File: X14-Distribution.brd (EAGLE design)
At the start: 152.4 x 76.2 mm, 57 parts, among them Q1 310mA/60V/1.6Ω, Q2 IRF1018EPBF, Q3 IRF1018EPBF, Q4 IRF1018EPBF, Q5 IRLML5203, Q6 IRLML5203, Q7 IRLML5203, Q8 IRLML5203, U1 DIST_OR_CONTROL_ALTMK06A-M, U2 DIST_OR_CONTROL_ALTMK06A-M

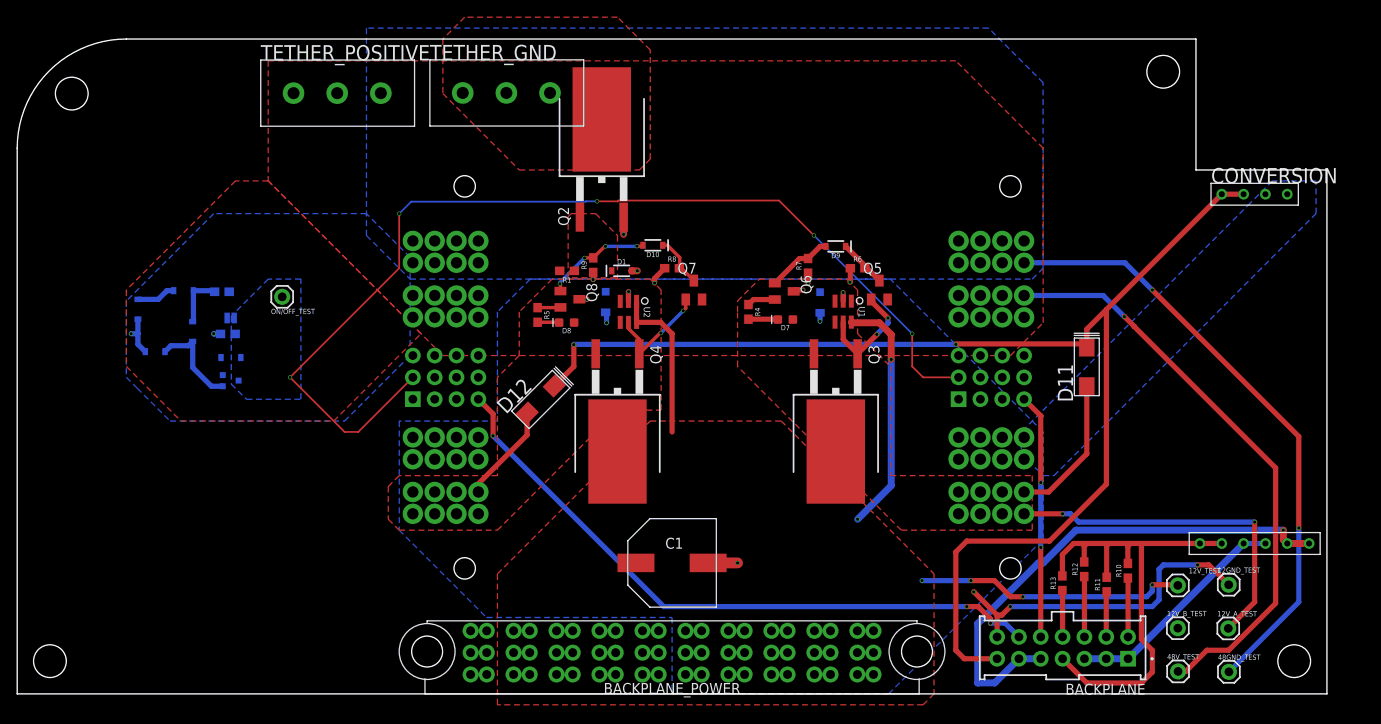
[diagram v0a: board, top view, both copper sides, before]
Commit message: Chagned some wires to make it fit DRC
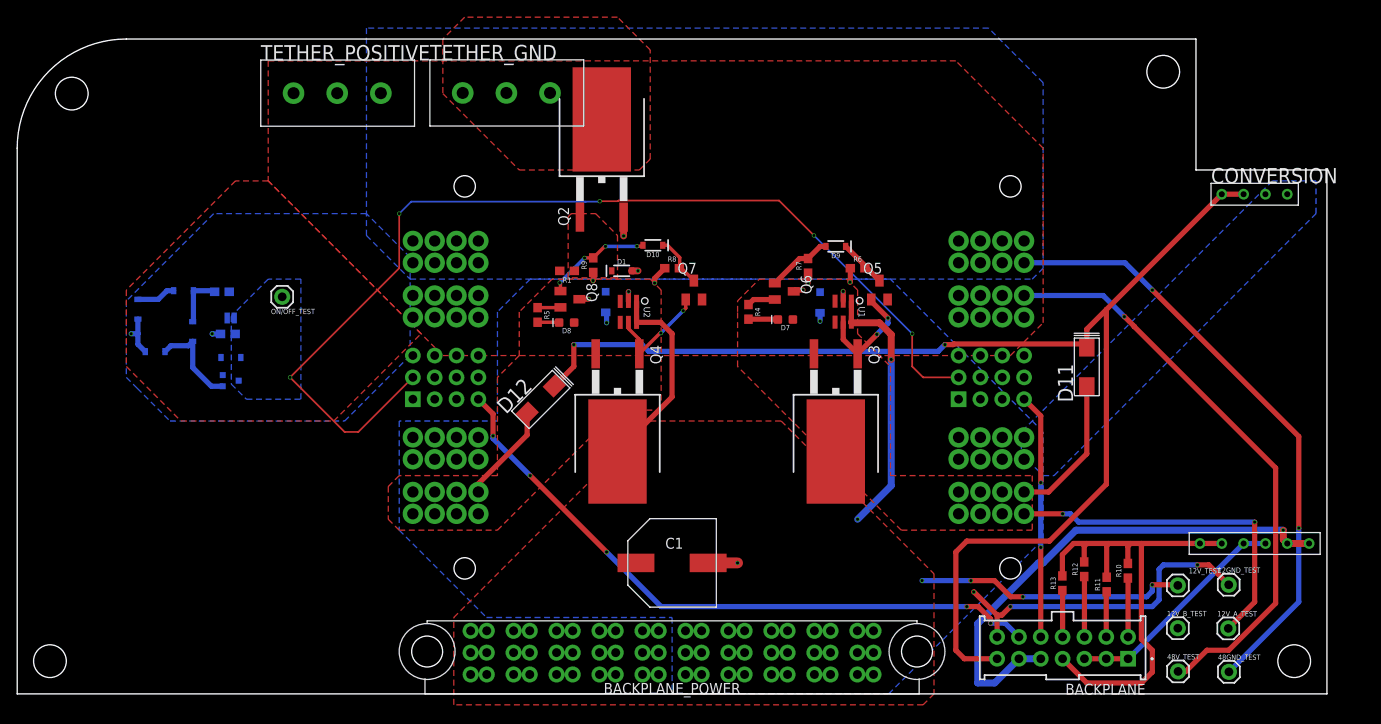
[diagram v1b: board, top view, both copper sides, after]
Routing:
- net +12V: track 78.5 -> 85.8 mm
- net +12V_CONV: track 150.2 -> 150.9 mm
- net C2_2: track 76.1 -> 76.3 mm, vias 3 -> 5

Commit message: Mad e more changes
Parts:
- moved Q3 2.05 mm to (93.2, 33.3)
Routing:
- net 12V_GND: track 52.7 -> 49.3 mm, vias 12 -> 30
- net 48V_GND: track 74.0 -> 71.8 mm, vias 4 -> 7
- net OR_DRIVE_A: track 13.0 -> 15.0 mm
- net +12V_B: track 12.8 -> 14.3 mm
- net C2_2: track 76.3 -> 75.9 mm, vias 5 -> 3
- added copper zone on layer 1, net 12V_GND
- added copper zone on layer 1, net 48V_GND

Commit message: Maybe done?
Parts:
- moved 12V_B_TEST 110.8 mm to (29.9, 42.4)
- moved R11 3.57 mm to (127.0, 16.3)
- moved R13 3.57 mm to (121.9, 16.4)
- moved R10 2.05 mm to (129.5, 16.4)
- moved R12 2.05 mm to (124.4, 16.5)
- moved ON/OFF_TEST 1.02 mm to (29.8, 46.2)
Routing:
- net DATA: track 6.86 -> 126.9 mm, vias 0 -> 3
- net ALERT_2: track 7.03 -> 115.5 mm, vias 0 -> 5
- net CLK: track 5.41 -> 111.4 mm, vias 0 -> 3
- net ALERT_1: track 5.27 -> 53.7 mm, vias 0 -> 1
- net +12V_A: track 58.9 -> 89.8 mm, vias 3 -> 7
- net +12V_B: track 14.3 -> 42.7 mm
- net C2_2: track 75.9 -> 94.1 mm, vias 3 -> 4
- net D_GND: track 59.8 -> 44.5 mm, vias 1 -> 0
- net +3.3V: track 57.9 -> 44.2 mm
- net 12V_GND: track 49.3 -> 58.7 mm
- net C2_1: track 28.5 -> 31.7 mm
- net +12V: track 85.8 -> 86.7 mm

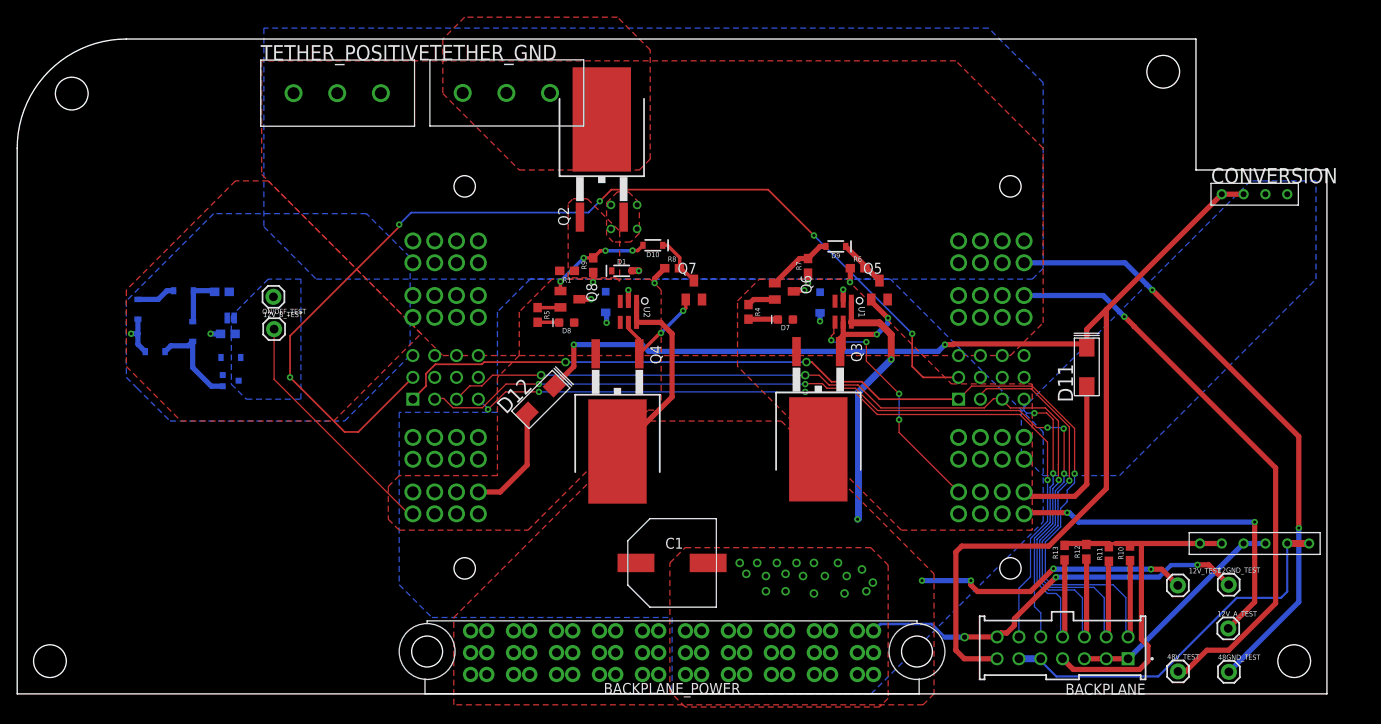
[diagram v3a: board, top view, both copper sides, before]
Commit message: moved on/off circuit
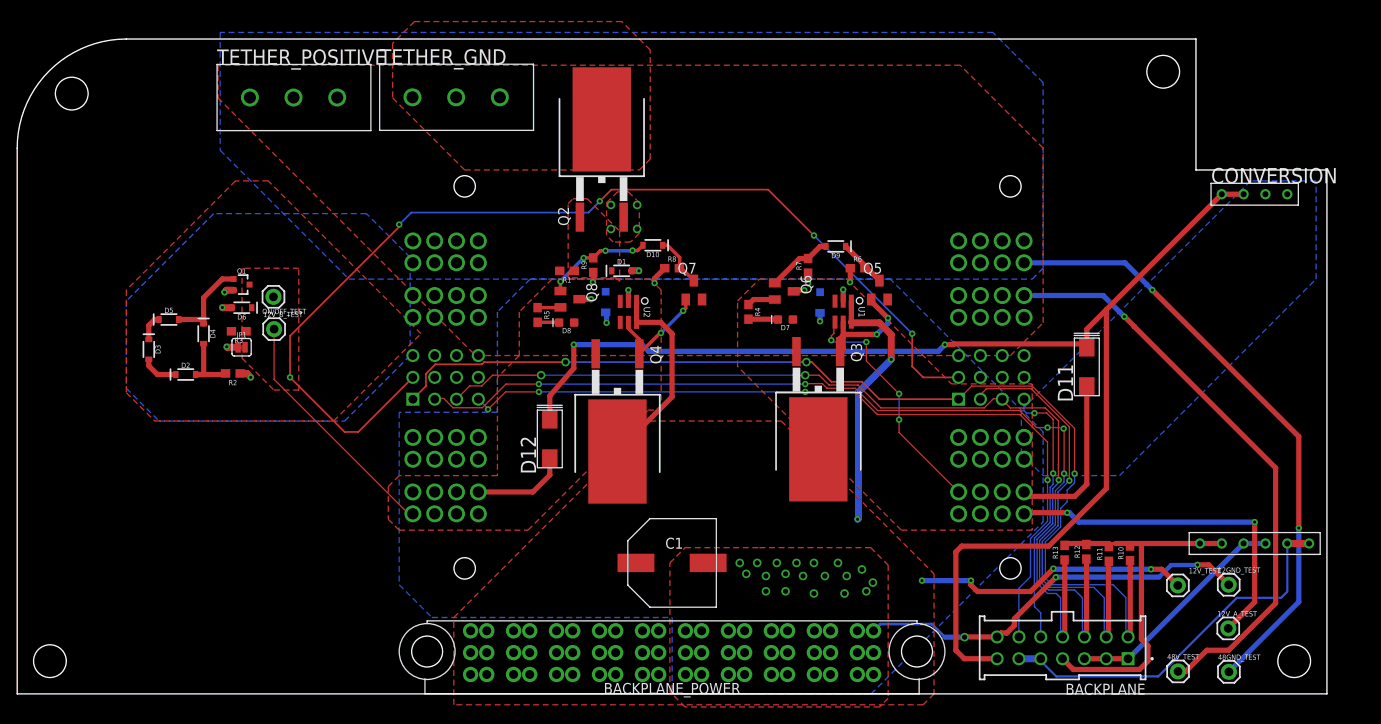
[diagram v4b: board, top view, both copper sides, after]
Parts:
- moved Q1 11.2 mm to (26.1, 47.6), flipped to the top, turned to 270 degrees
- moved D2 9.76 mm to (19.6, 37.2), flipped to the top, turned to 0 degrees
- moved R2 9.58 mm to (25.1, 37.3), flipped to the top, turned to 180 degrees
- moved D6 5.93 mm to (26.1, 44.9), flipped to the top, turned to 180 degrees
- moved TETHER_GND 5.86 mm to (51.1, 69.4)
- moved TETHER_POSITIVE 5.11 mm to (32.2, 69.4)
- moved D3 4.84 mm to (15.3, 40.1), flipped to the top, turned to 270 degrees
- moved D12 4.68 mm to (62.0, 29.7), turned to 90 degrees
- moved D5 4.06 mm to (17.7, 43.6), flipped to the top, turned to 0 degrees
- moved JP1 3.63 mm to (26.1, 40.3), flipped to the top, turned to 0 degrees
- moved R3 1.31 mm to (25.8, 42.2), flipped to the top, turned to 180 degrees
- moved D4 1.30 mm to (21.7, 41.9), flipped to the top, turned to 270 degrees
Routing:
- net 48V_GND: track 72.0 -> 77.0 mm, vias 7 -> 11
- net +12V_CONV: track 151.2 -> 155.2 mm
- net +48V: track 74.1 -> 71.2 mm, vias 3 -> 1
- net +12V_B: track 42.7 -> 40.8 mm
- net N$6: track 6.16 -> 8.07 mm
- added copper zone on layer 1, net ON/OFF
- removed copper zone on layer 16, net ON/OFF

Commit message: Length-matched the DATA and CLK lines
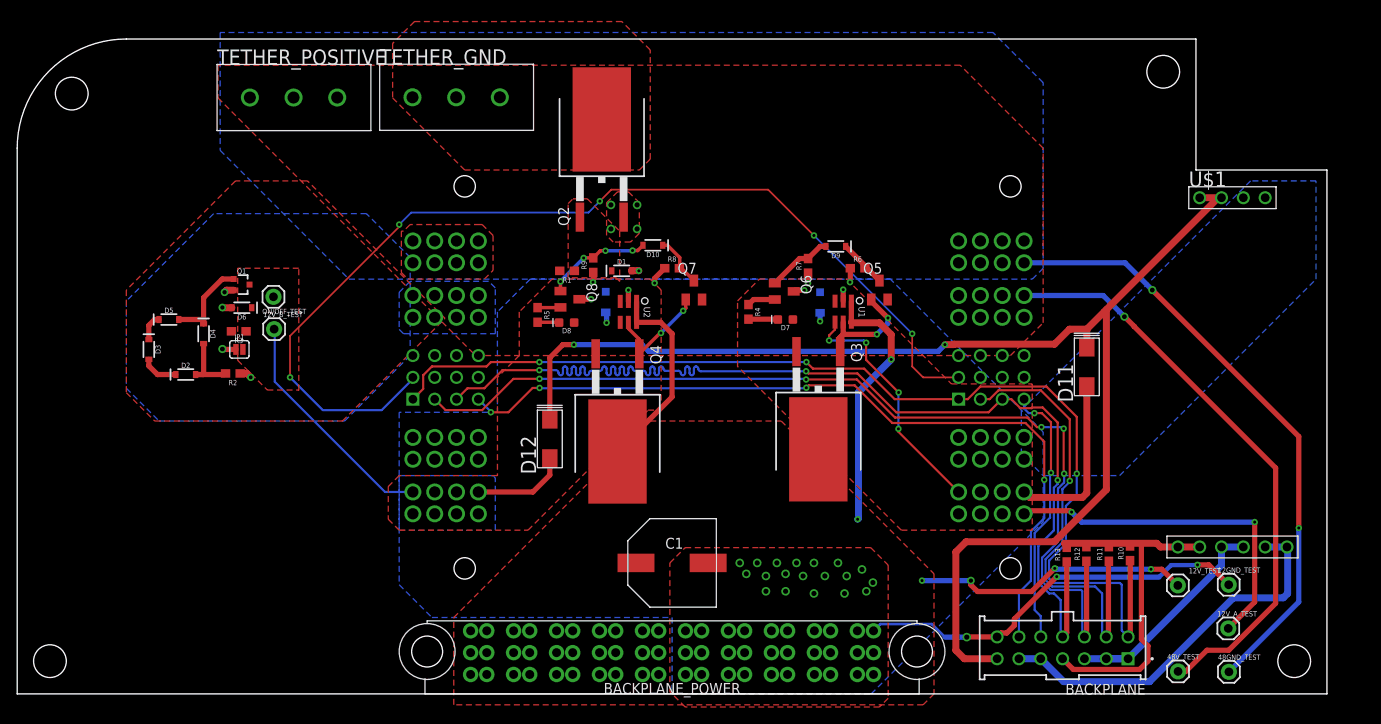
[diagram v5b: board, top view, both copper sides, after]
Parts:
- removed CONVERSION: DISTRIBUTION-CONVERSION, CONN, Distribution-Conversion:TSW-105-05-G-S(D-C)
- added U$1: DISTRIBUTION-CONVERSION, CONN, Distribution-Conversion:TSW-105-05-G-S(D-C)
- moved JP1 0.36 mm to (25.9, 40.1)
- moved R13 0.34 mm to (122.1, 16.2)
- moved R12 0.25 mm to (124.4, 16.3)
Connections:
- net +12V_CONV: now also U$1.1, U$1.2; no longer CONVERSION.1, CONVERSION.2
- net +3.3V: now also U$1.5, U$1.6; no longer CONVERSION.5, CONVERSION.6
- net +5V: now also U$1.7, U$1.8; no longer CONVERSION.7, CONVERSION.8
- net 12V_GND: now also U$1.3, U$1.4; no longer CONVERSION.3, CONVERSION.4
- net D_GND: now also U$1.10, U$1.9; no longer CONVERSION.10, CONVERSION.9
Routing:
- net CLK: track 111.4 -> 126.2 mm
- net +3.3V: track 44.2 -> 51.2 mm
- net ON/OFF: track 120.6 -> 118.6 mm
- net +12V_CONV: track 155.2 -> 156.5 mm
- net +12V_A: track 89.8 -> 91.0 mm
- net DATA: track 126.9 -> 128.1 mm
- net +5V: track 26.6 -> 27.7 mm
- net +12V_B: track 40.8 -> 39.9 mm
- net C2_1: track 31.7 -> 30.9 mm
- added copper zone on layer 1, net CUTOUT
- added copper zone on layer 16, net CUTOUT

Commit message: Made more changes to the board
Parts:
- moved C1 11.8 mm to (81.6, 25.8), turned to 90 degrees
- moved Q3 0.76 mm to (94.0, 33.3)
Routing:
- net OR_DRIVE_A: track 15.1 -> 13.4 mm
- net CLK: track 126.2 -> 127.6 mm
- net +12V_A: track 91.0 -> 90.0 mm
- net 12V_GND: vias 30 -> 11
- removed copper zone on layer 1, net 12V_GND

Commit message: Made a few more changes to the same board
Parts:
- moved C1 0.48 mm to (82.0, 25.5)
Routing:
- net 12V_GND: track 58.7 -> 63.3 mm, vias 11 -> 12
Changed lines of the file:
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@@
 <attribute name="NAME" x="76.2" y="0" size="1.27" layer="25" align="bottom-center"/>
 </element>
-<element name="C1" library="CAP, aluminin-capacitor-brick-UCM1H331MNL1GS" package="CAPAE1030X1050N" package3d_urn="urn:adsk.eagle:package:24202090/2" value="330uF" x="81.5594" y="25.781" smashed="yes" rot="R90">
-<attribute name="ARROW_PART_NUMBER" value="UCM1H331MNL1GS" x="142.5194" y="110.871" size="1.778" layer="27" rot="R90" display="off"/>
-<attribute name="ARROW_PRICE-STOCK" value="https://www.arrow.com/en/products/ucm1h331mnl1gs/nichicon" x="142.5194" y="110.871" size="1.778" layer="27" rot="R90" display="off"/>
-<attribute name="DESCRIPTION" value="Nichicon 330uF 50 V Aluminium Electrolytic Capacitor SMD, CM Series 2000h 10 (Dia.) x 10mm" x="142.5194" y="110.871" size="1.778" layer="27" rot="R90" display="off"/>
-<attribute name="HEIGHT" value="10.5mm" x="142.5194" y="110.871" size="1.778" layer="27" rot="R90" display="off"/>
-<attribute name="MANUFACTURER_NAME" value="Nichicon" x="142.5194" y="110.871" size="1.778" layer="27" rot="R90" display="off"/>
-<attribute name="MANUFACTURER_PART_NUMBER" value="UCM1H331MNL1GS" x="142.5194" y="110.871" size="1.778" layer="27" rot="R90" display="off"/>
-<attribute name="MOUSER_PART_NUMBER" value="647-UCM1H331MNL1GS" x="142.5194" y="110.871" size="1.778" layer="27" rot="R90" display="off"/>
-<attribute name="MOUSER_PRICE-STOCK" value="https://www.mouser.co.uk/ProductDetail/Nichicon/UCM1H331MNL1GS?qs=DSgADHjnLTkTovFLdbC%252BNg%3D%3D" x="142.5194" y="110.871" size="1.778" layer="27" rot="R90" display="off"/>
-<attribute name="NAME" x="79.2734" y="26.035" size="1.27" layer="25" rot="R90" align="center"/>
-<attribute name="VALUE" x="84.0994" y="25.781" size="1.27" layer="27" rot="R90" align="center"/>
+<element name="C1" library="CAP, aluminin-capacitor-brick-UCM1H331MNL1GS" package="CAPAE1030X1050N" package3d_urn="urn:adsk.eagle:package:24202090/2" value="330uF" x="81.9658" y="25.527" smashed="yes" rot="R90">
+<attribute name="ARROW_PART_NUMBER" value="UCM1H331MNL1GS" x="142.9258" y="110.617" size="1.778" layer="27" rot="R90" display="off"/>
+<attribute name="ARROW_PRICE-STOCK" value="https://www.arrow.com/en/products/ucm1h331mnl1gs/nichicon" x="142.9258" y="110.617" size="1.778" layer="27" rot="R90" display="off"/>
+<attribute name="DESCRIPTION" value="Nichicon 330uF 50 V Aluminium Electrolytic Capacitor SMD, CM Series 2000h 10 (Dia.) x 10mm" x="142.9258" y="110.617" size="1.778" layer="27" rot="R90" display="off"/>
+<attribute name="HEIGHT" value="10.5mm" x="142.9258" y="110.617" size="1.778" layer="27" rot="R90" display="off"/>
+<attribute name="MANUFACTURER_NAME" value="Nichicon" x="142.9258" y="110.617" size="1.778" layer="27" rot="R90" display="off"/>
+<attribute name="MANUFACTURER_PART_NUMBER" value="UCM1H331MNL1GS" x="142.9258" y="110.617" size="1.778" layer="27" rot="R90" display="off"/>
+<attribute name="MOUSER_PART_NUMBER" value="647-UCM1H331MNL1GS" x="142.9258" y="110.617" size="1.778" layer="27" rot="R90" display="off"/>
+<attribute name="MOUSER_PRICE-STOCK" value="https://www.mouser.co.uk/ProductDetail/Nichicon/UCM1H331MNL1GS?qs=DSgADHjnLTkTovFLdbC%252BNg%3D%3D" x="142.9258" y="110.617" size="1.778" layer="27" rot="R90" display="off"/>
+<attribute name="NAME" x="79.6798" y="25.781" size="1.27" layer="25" rot="R90" align="center"/>
+<attribute name="VALUE" x="84.5058" y="25.527" size="1.27" layer="27" rot="R90" align="center"/>
 </element>
 <element name="D1" library="SparkFun-DiscreteSemi" library_urn="urn:adsk.eagle:library:514" package="SOD-323" package3d_urn="urn:adsk.eagle:package:38441/1" value="15V" x="70.3326" y="49.2252" smashed="yes">
@@
 <via x="105.283" y="13.1826" extent="1-16" drill="0.65"/>
 <wire x1="120.7262" y1="14.605" x2="118.0338" y2="11.9126" width="0.6096" layer="1"/>
-<wire x1="118.0338" y1="11.9126" x2="111.7346" y2="11.9126" width="0.6096" layer="1"/>
-<wire x1="111.7346" y1="11.9126" x2="110.9726" y2="12.6746" width="0.6096" layer="1"/>
-<wire x1="110.9726" y1="12.6746" x2="110.9726" y2="13.1826" width="0.6096" layer="1"/>
+<wire x1="118.0338" y1="11.9126" x2="112.2426" y2="11.9126" width="0.6096" layer="1"/>
+<wire x1="112.2426" y1="11.9126" x2="110.9726" y2="13.1826" width="0.6096" layer="1"/>
 <wire x1="72.07" y1="43.2308" x2="74.8792" y2="43.2308" width="0.6096" layer="1"/>
 <wire x1="76.2" y1="41.91" x2="74.8792" y2="43.2308" width="0.6096" layer="1"/>
@@
 <contactref element="U$1" pad="4"/>
 <contactref element="U$1" pad="3"/>
-<wire x1="71.12" y1="45.6692" x2="81.5594" y2="29.981" width="0" layer="19" extent="1-1"/>
+<wire x1="81.9658" y1="29.727" x2="81.9658" y2="34.2646" width="1.016" layer="1"/>
+<wire x1="81.9658" y1="34.2646" x2="81.9404" y2="34.29" width="1.016" layer="1"/>
+<via x="81.9404" y="34.29" extent="1-16" drill="0.75"/>
 </signal>
 <signal name="N$5">
@@
 <contactref element="BRICKS1" pad="01"/>
 <contactref element="BRICKS2" pad="01"/>
-<wire x1="129.5146" y1="15.4822" x2="129.4892" y2="15.5076" width="0.4064" layer="1"/>
 <wire x1="129.2606" y1="6.6294" x2="129.5146" y2="6.8834" width="0.254" layer="1"/>
 <wire x1="129.5146" y1="15.4822" x2="129.5146" y2="6.8834" width="0.254" layer="1"/>
@@
 <wire x1="120.0686" y1="15.5123875" x2="122.0244" y2="17.4681875" width="0.254" layer="16"/>
 <wire x1="122.0244" y1="17.4681875" x2="122.0244" y2="21.8623875" width="0.254" layer="16"/>
+<wire x1="129.4892" y1="15.5076" x2="129.5146" y2="15.4822" width="0.254" layer="1"/>
 </signal>
 <signal name="CLK">
@@
 <contactref element="BRICKS1" pad="03"/>
 <contactref element="BRICKS2" pad="03"/>
-<wire x1="122.1232" y1="15.3552" x2="122.1232" y2="7.112" width="0.254" layer="1"/>
-<wire x1="121.6406" y1="6.6294" x2="122.1232" y2="7.112" width="0.254" layer="1"/>
+<wire x1="122.1232" y1="7.112" x2="121.6406" y2="6.6294" width="0.254" layer="1"/>
 <via x="60.7568" y="37.6682" extent="1-16" drill="0.35"/>
 <wire x1="56.4642" y1="37.6682" x2="60.7568" y2="37.6682" width="0.254" layer="1"/>
@@
 <wire x1="120.396" y1="10.414" x2="120.142" y2="10.668" width="0.254" layer="16" curve="-90"/>
 <wire x1="120.142" y1="10.668" x2="120.142" y2="11.6206" width="0.254" layer="16"/>
+<wire x1="122.1232" y1="15.3552" x2="122.1232" y2="7.112" width="0.254" layer="1"/>
 </signal>
 <signal name="+3.3V">
@@
 <contactref element="R13" pad="2"/>
 <contactref element="BACKPLANE" pad="04"/>
-<wire x1="130.81" y1="17.5006" x2="129.54" y2="17.5006" width="0.6096" layer="1"/>
-<wire x1="129.54" y1="17.5006" x2="127.7874" y2="17.5006" width="0.6096" layer="1"/>
+<wire x1="130.81" y1="17.5006" x2="129.1962" y2="17.5006" width="0.6096" layer="1"/>
+<wire x1="129.1962" y1="17.5006" x2="127.7874" y2="17.5006" width="0.6096" layer="1"/>
 <wire x1="124.46" y1="17.5006" x2="127" y2="17.5006" width="0.6096" layer="1"/>
 <wire x1="124.46" y1="17.5006" x2="122.1232" y2="17.5006" width="0.6096" layer="1"/>
@@
 <wire x1="124.4092" y1="17.4498" x2="124.46" y2="17.5006" width="0.6096" layer="1"/>
 <wire x1="127.0254" y1="17.1314" x2="127.0254" y2="17.5006" width="0.6096" layer="1"/>
-<wire x1="129.4892" y1="17.2076" x2="129.4892" y2="17.4498" width="0.6096" layer="1"/>
-<wire x1="129.4892" y1="17.4498" x2="129.54" y2="17.5006" width="0.6096" layer="1"/>
+<wire x1="129.4892" y1="17.2076" x2="129.1962" y2="17.5006" width="0.6096" layer="1"/>
 <wire x1="130.81" y1="17.5006" x2="130.81" y2="6.35" width="0.6096" layer="1"/>
 <wire x1="130.81" y1="6.35" x2="131.572" y2="5.588" width="0.6096" layer="1"/>
